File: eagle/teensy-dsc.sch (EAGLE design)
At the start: 27 parts, among them J1 RJ11-6PTH, J2 RJ11-6PTH, J3 RJ45-8PTH, J4 POWER_JACKPTH, M1 XBEERX-VN, Q1 IRLML6344, X1 STEREOJACK, X2 STEREOJACK

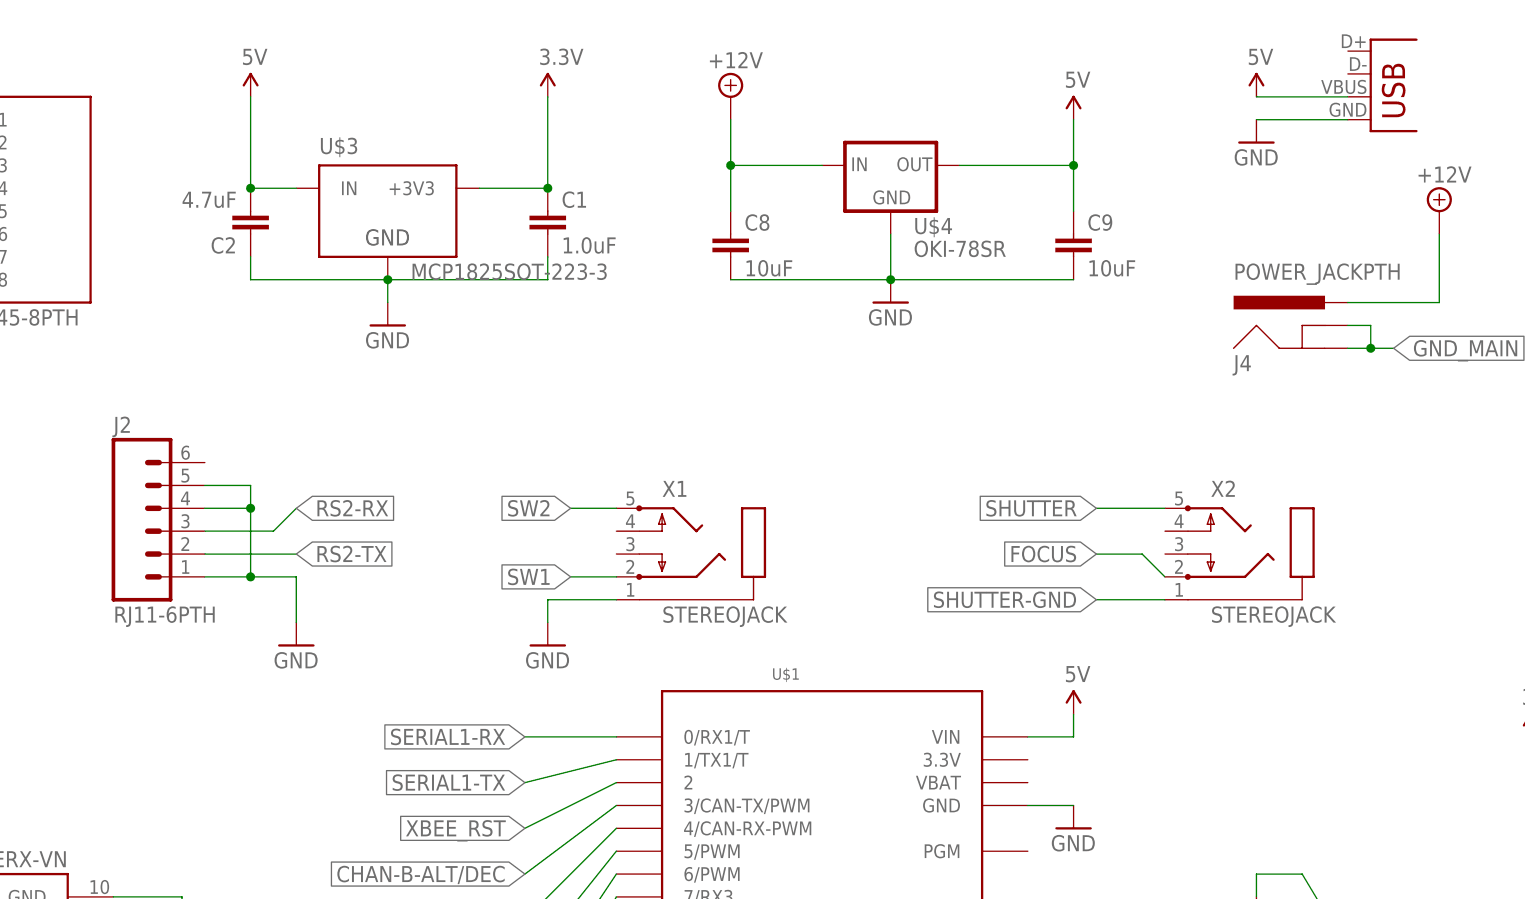
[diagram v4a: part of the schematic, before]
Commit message: Fix power error in .sch Update board to theoretically fit in CU-789 box
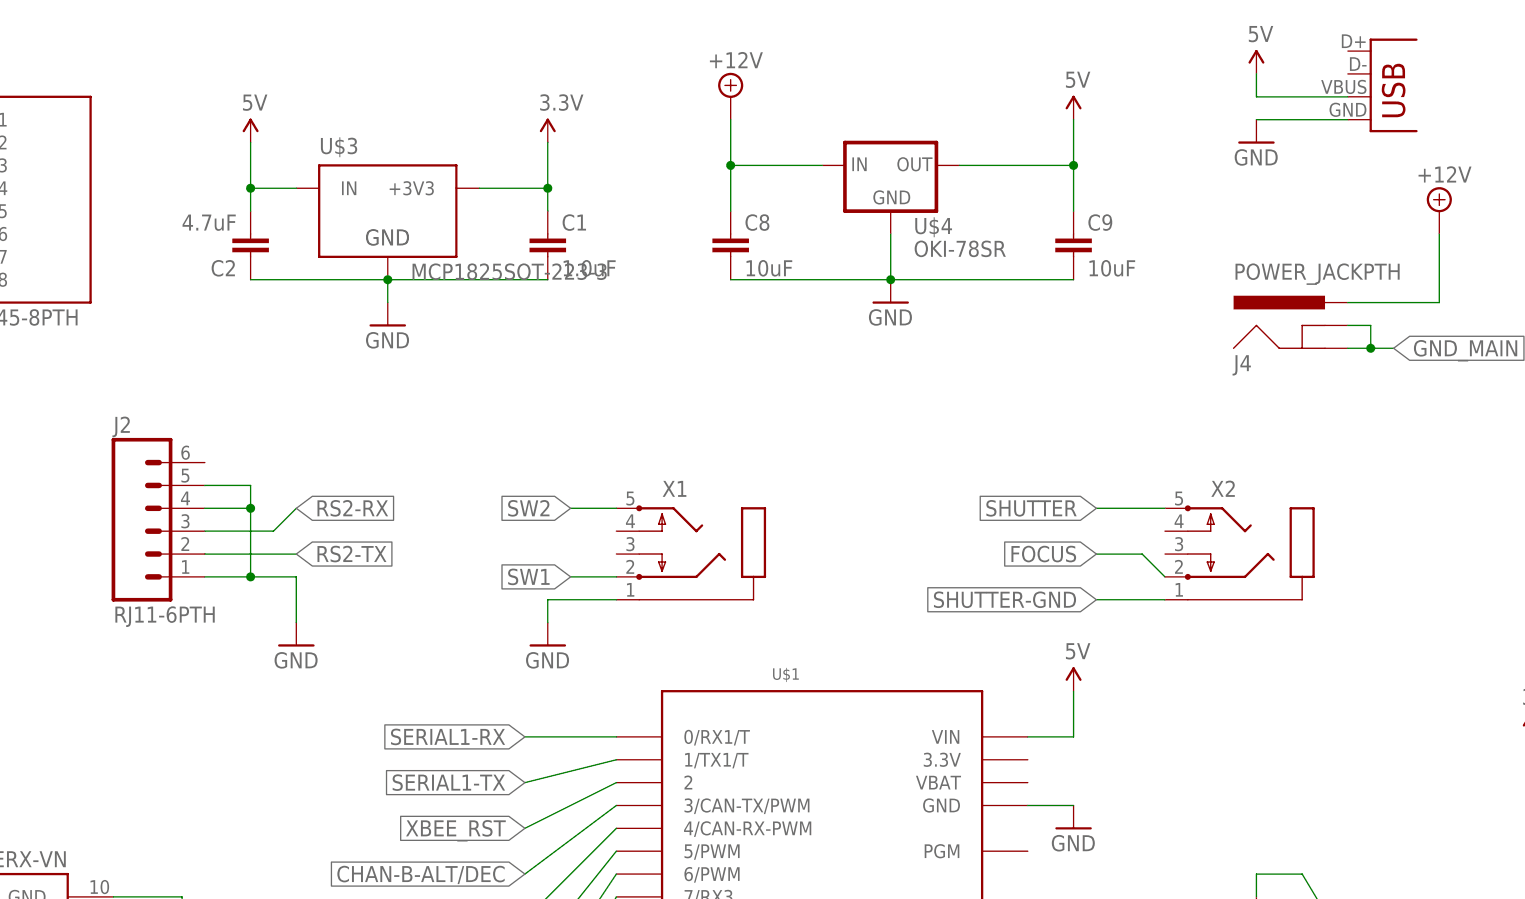
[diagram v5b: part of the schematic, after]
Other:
- moved on the sheet: C1, C2

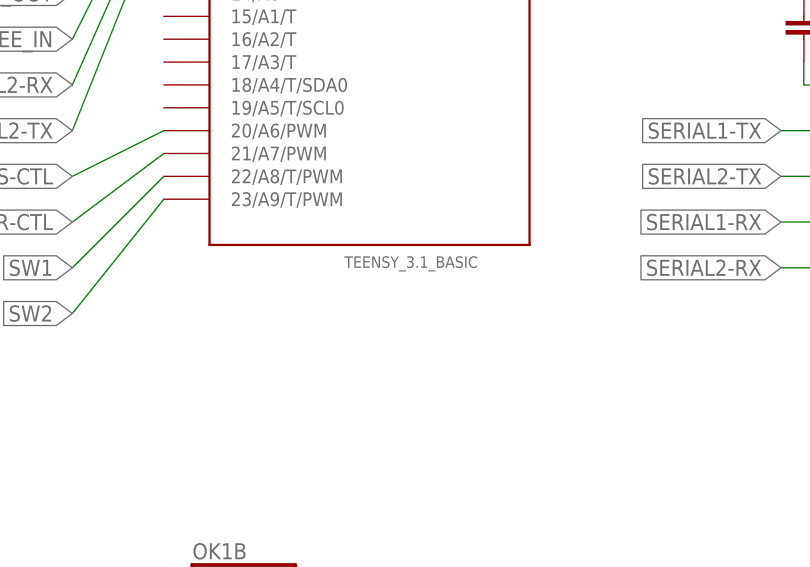
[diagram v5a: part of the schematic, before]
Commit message: Lots of changes:
- Start working on a CLI framework
- Update Commands & Readme docs
- Note on the Eagle file that we need to cut the VUSB/VIN pads apart
- Re-organize some header files
- general cleanup
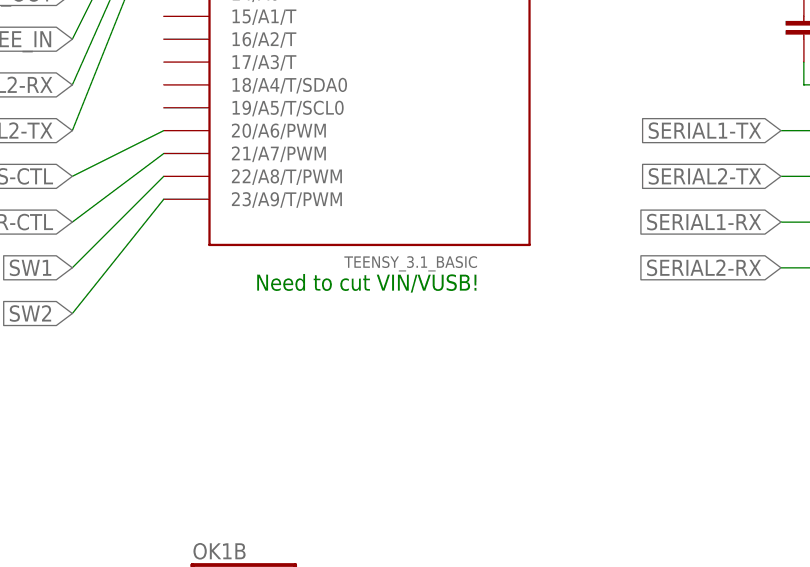
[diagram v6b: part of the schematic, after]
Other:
- note added: "Need to cut VIN/VUSB!"
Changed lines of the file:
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@@
 http://synfin.net/teensydsc</text>
 <text x="160.02" y="-20.32" size="2.1844" layer="90">v0.3</text>
+<text x="25.4" y="30.48" size="1.778" layer="91">Need to cut VIN/VUSB!</text>
 </plain>
 <instances>

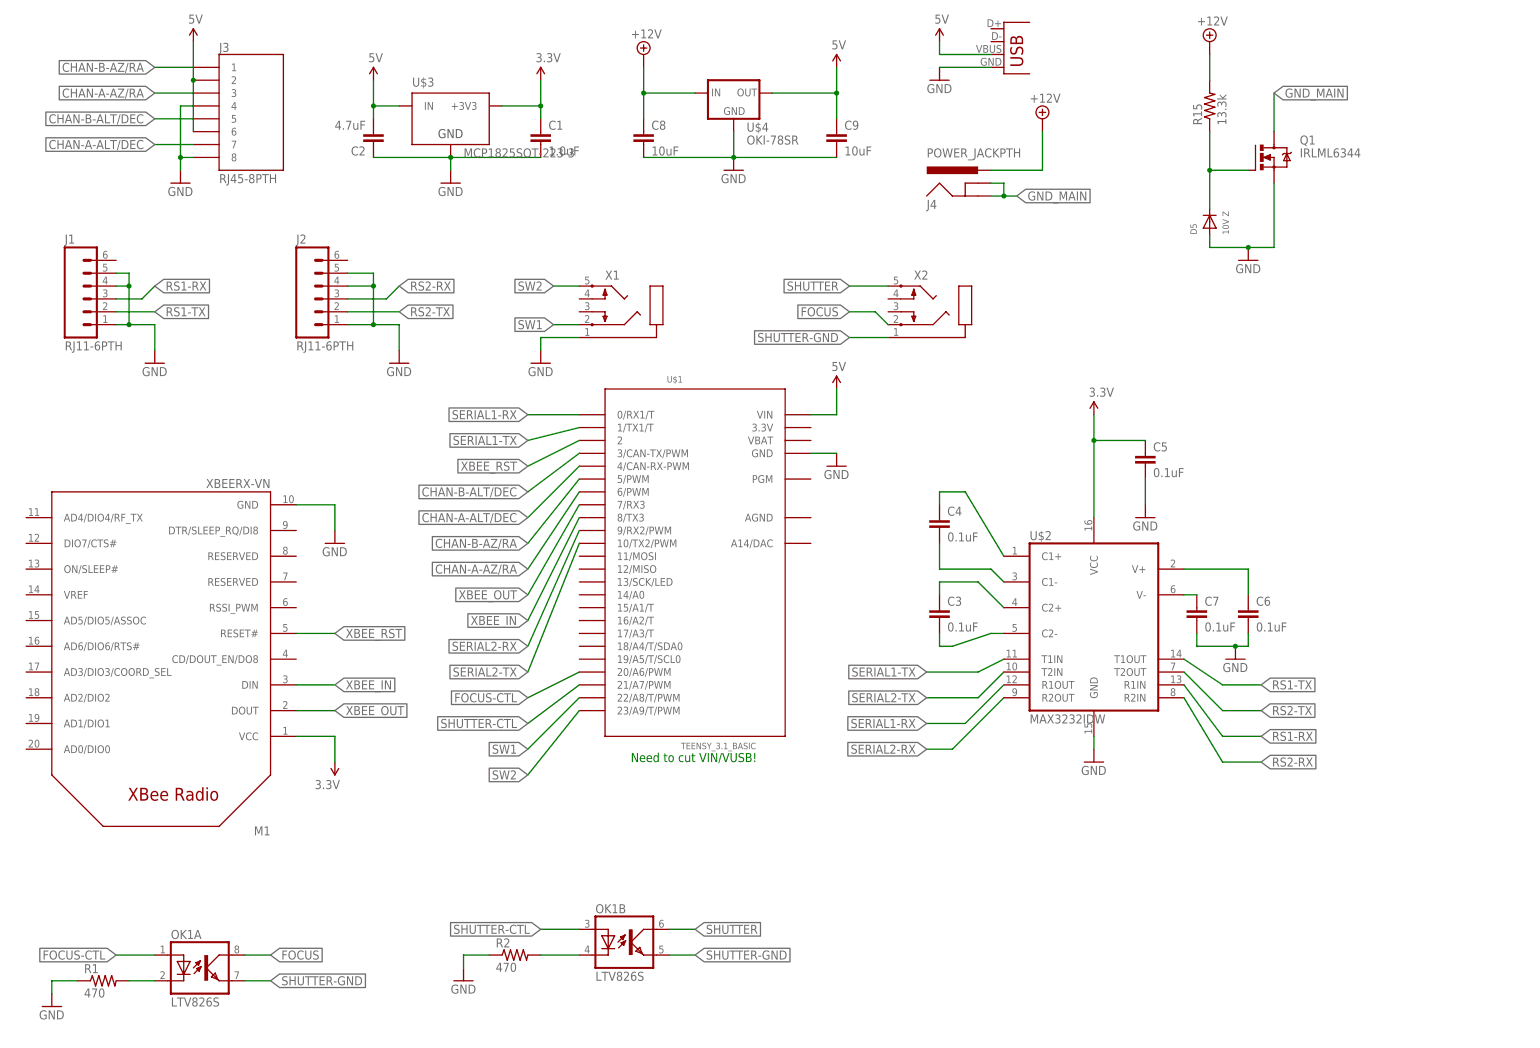
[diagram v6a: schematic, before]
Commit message: v0.5 simple board/just DSC functionality
No serial, camera, etc.
Has USB & 12V power input options
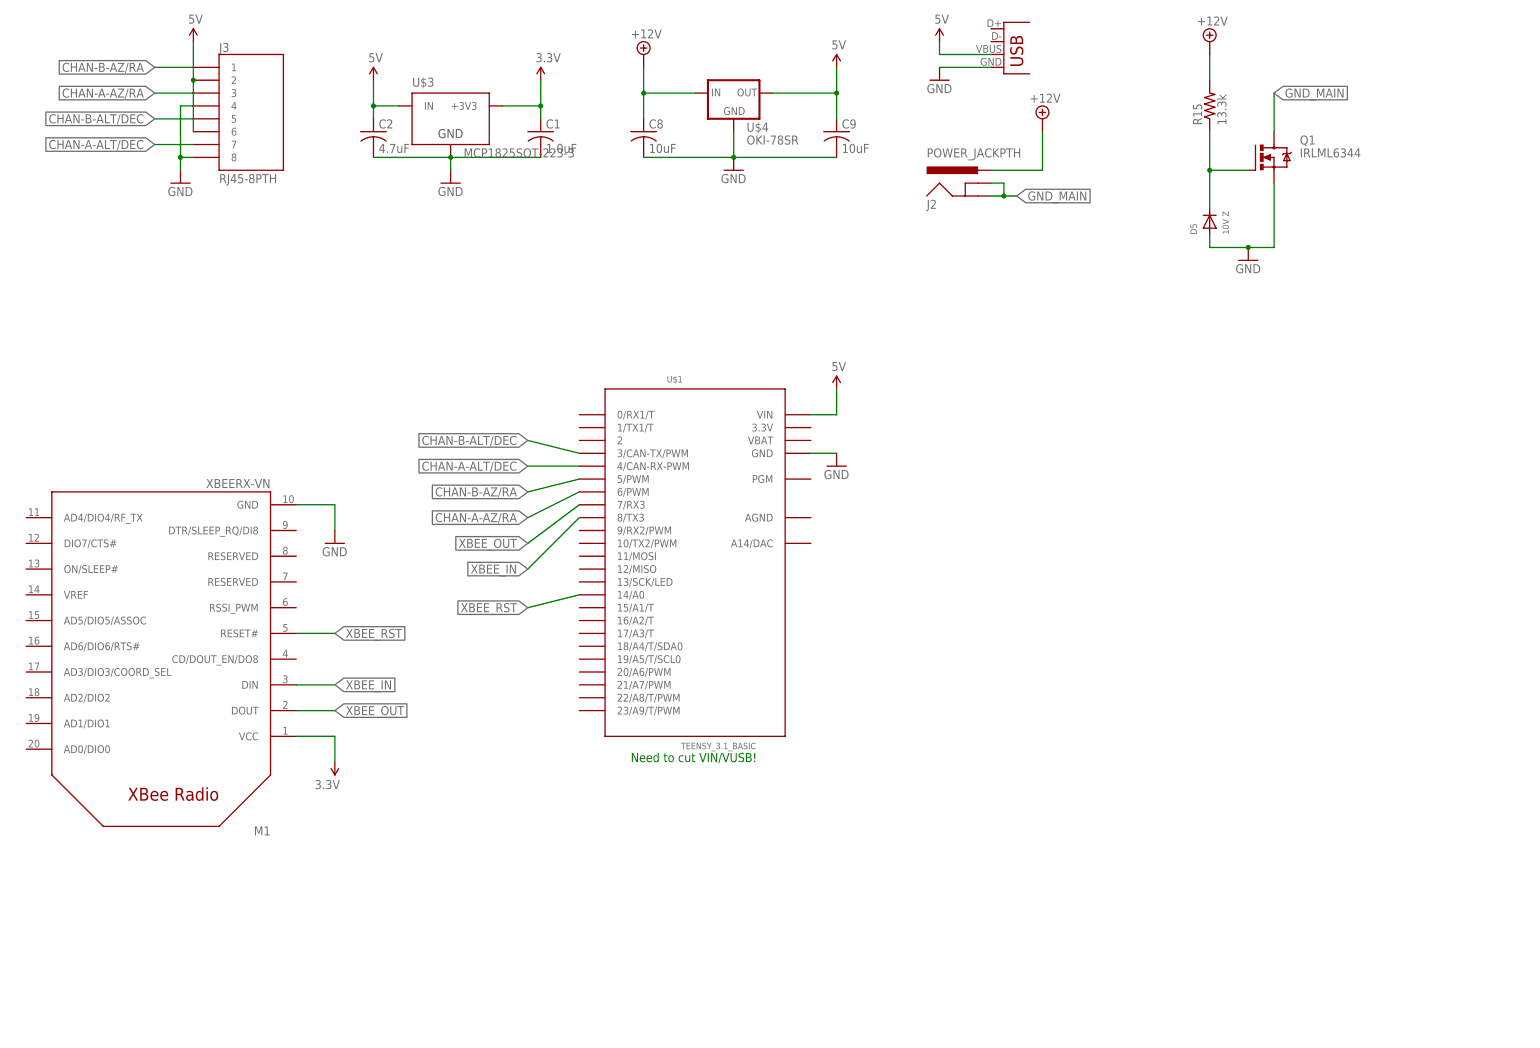
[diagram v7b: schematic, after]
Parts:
- removed C3, C4, C5, C6, C7: 0.1uF, SparkFun-Passives:CAP0805
- removed J4: POWER_JACKPTH, SparkFun-Connectors:POWER_JACKPTH
- removed JP1: USB-B, SparkFun-Connectors:USBPTH
- removed OK1: LTV826S, optocoupler:LTV826S
- removed R1, R2: 470, SparkFun-Resistors:0.75OHM1/4W1%(0805)
- removed U$2: MAX3232IDW, SparkFun-DigitalIC:MAX232SOIC16
- removed X1, X2: STEREOJACK, adafruit:STEREOJACK
- C1: device SparkFun-Capacitors:1.0UF-25V-+80/-20(0805) -> resistor:C-USC0805
- C2: device SparkFun-Capacitors:22UF-6.3V-20%(0805) -> resistor:C-USC0805
- C8, C9: device resistor:C-EUC0805 -> resistor:C-USC0805
- J1: value RJ11-6PTH -> USB-B; device SparkFun-Connectors:RJ11-6PTH -> SparkFun-Connectors:USBPTH
- J2: value RJ11-6PTH -> POWER_JACKPTH; device SparkFun-Connectors:RJ11-6PTH -> SparkFun-Connectors:POWER_JACKPTH
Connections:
- removed net FOCUS: OK1A.COL, X2.2
- removed net FOCUS-CTL: OK1A.A, U$1.20/A6/PWM
- removed net N$1: C4.1, U$2.C1+
- removed net N$2: C4.2, U$2.C1-
- removed net N$3: C3.1, U$2.C2+
- removed net N$4: C3.2, U$2.C2-
- removed net N$5: C7.1, U$2.V-
- removed net N$6: C6.1, U$2.V+
- removed net N$7: OK1B.C, R2.2
- removed net N$9: OK1A.C, R1.2
- removed net RS1-RX: J1.3, U$2.R1IN
- removed net RS1-TX: J1.2, U$2.T1OUT
- removed net RS2-RX: J2.3, U$2.R2IN
- removed net RS2-TX: J2.2, U$2.T2OUT
- removed net SERIAL1-RX: U$1.0/RX1/T, U$2.R1OUT
- removed net SERIAL1-TX: U$1.1/TX1/T, U$2.T1IN
- removed net SERIAL2-RX: U$1.9/RX2/PWM, U$2.R2OUT
- removed net SERIAL2-TX: U$1.10/TX2/PWM, U$2.T2IN
- removed net SHUTTER: OK1B.COL, X2.5
- removed net SHUTTER-CTL: OK1B.A, U$1.21/A7/PWM
- removed net SHUTTER-GND: OK1A.EMIT, OK1B.EMIT, X2.1
- removed net SW1: U$1.22/A8/T/PWM, X1.2
- removed net SW2: U$1.23/A9/T/PWM, X1.5
- net +12V: now also J2.PWR; no longer J4.PWR
- net 3.3V: no longer C5.1, U$2.VCC
- net 5V: now also C2.1, J1.VBUS; no longer C2.2, JP1.VBUS
- net GND: now also C2.2, J1.GND; no longer C2.1, C5.2, C6.2, C7.2, J1.1, J1.4, J1.5, J2.1, J2.4, J2.5, JP1.GND, R1.1, R2.1, U$2.GND, X1.1
- net GND_MAIN: now also J2.GND, J2.GNDBREAK; no longer J4.GND, J4.GNDBREAK
- net XBEE_RST: now also U$1.14/A0; no longer U$1.2
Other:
- note added: "v0.5"
- note removed: "v0.3"
- moved on the sheet: C2

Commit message: update date on brd to be a valid date update version on sch to match the brd
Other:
- note added: "v0.5.1"
- note removed: "v0.5"
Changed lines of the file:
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@@
 <?xml version="1.0" encoding="utf-8"?>
 <!DOCTYPE eagle SYSTEM "eagle.dtd">
-<eagle version="7.1.0">
+<eagle version="7.2.0">
 <drawing>
 <settings>
@@
 <text x="71.12" y="-2.54" size="3.81" layer="90">Aaron Turner
 http://synfin.net/teensydsc</text>
-<text x="160.02" y="-20.32" size="2.1844" layer="90">v0.5</text>
+<text x="160.02" y="-20.32" size="2.1844" layer="90">v0.5.1</text>
 <text x="25.4" y="30.48" size="1.778" layer="91">Need to cut VIN/VUSB!</text>
 </plain>
